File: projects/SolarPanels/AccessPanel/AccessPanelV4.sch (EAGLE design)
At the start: 39 parts

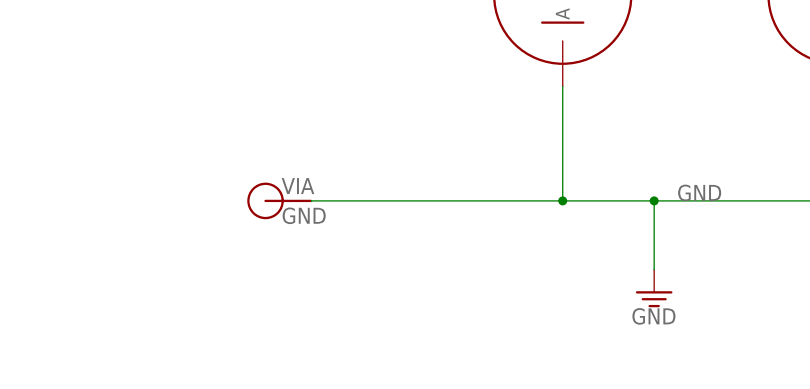
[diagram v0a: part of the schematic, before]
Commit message: Additional edits to Access Panel V4 layout. Just needs the access connector.
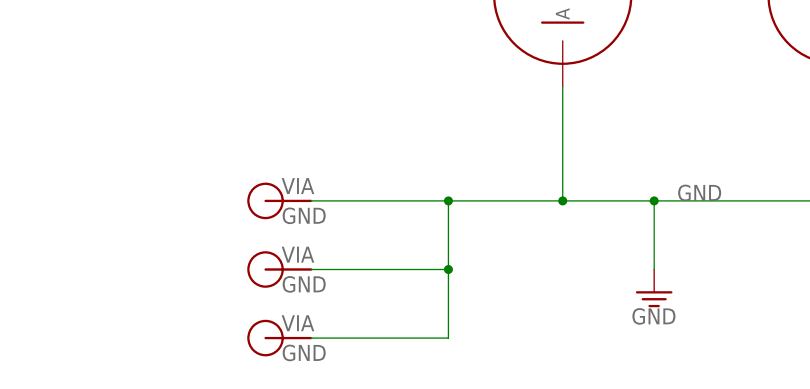
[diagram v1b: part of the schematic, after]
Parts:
- added V2, V5: GND, BrownSpaceEngineering:VIA-60MIL
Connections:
- net GND: now also V2.P$1, V5.P$1
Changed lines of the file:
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@@
 <part name="D1" library="BrownSpaceEngineering" deviceset="DFLS130L" device="" value="DFLS130L"/>
 <part name="R1" library="BrownSpaceEngineering" deviceset="RES" device="1210" value="0R"/>
+<part name="V2" library="BrownSpaceEngineering" deviceset="VIA" device="-60MIL" value="GND"/>
+<part name="V5" library="BrownSpaceEngineering" deviceset="VIA" device="-60MIL" value="GND"/>
 </parts>
 <sheets>
@@
 <instance part="D1" gate="G$1" x="172.72" y="40.64"/>
 <instance part="R1" gate="R$1" x="175.26" y="30.48"/>
+<instance part="V2" gate="G$1" x="-60.96" y="-93.98"/>
+<instance part="V5" gate="G$1" x="-60.96" y="-101.6"/>
 </instances>
 <busses>
@@
 <junction x="127" y="-86.36"/>
 <pinref part="V4" gate="G$1" pin="P$1"/>
-<wire x1="-55.88" y1="-86.36" x2="-27.94" y2="-86.36" width="0.1524" layer="91"/>
+<wire x1="-55.88" y1="-86.36" x2="-40.64" y2="-86.36" width="0.1524" layer="91"/>
 <junction x="-27.94" y="-86.36"/>
 <pinref part="GND1" gate="1" pin="GND"/>
+<wire x1="-40.64" y1="-86.36" x2="-27.94" y2="-86.36" width="0.1524" layer="91"/>
 <wire x1="-17.78" y1="-93.98" x2="-17.78" y2="-86.36" width="0.1524" layer="91"/>
 <junction x="-17.78" y="-86.36"/>
-</segment>
-<segment>
+<pinref part="V5" gate="G$1" pin="P$1"/>
+<wire x1="-55.88" y1="-101.6" x2="-40.64" y2="-101.6" width="0.1524" layer="91"/>
+<wire x1="-40.64" y1="-101.6" x2="-40.64" y2="-93.98" width="0.1524" layer="91"/>
+<junction x="-40.64" y="-86.36"/>
+<pinref part="V2" gate="G$1" pin="P$1"/>
+<wire x1="-40.64" y1="-93.98" x2="-40.64" y2="-86.36" width="0.1524" layer="91"/>
+<wire x1="-55.88" y1="-93.98" x2="-40.64" y2="-93.98" width="0.1524" layer="91"/>
+<junction x="-40.64" y="-93.98"/>
+</segment>
+<segment>

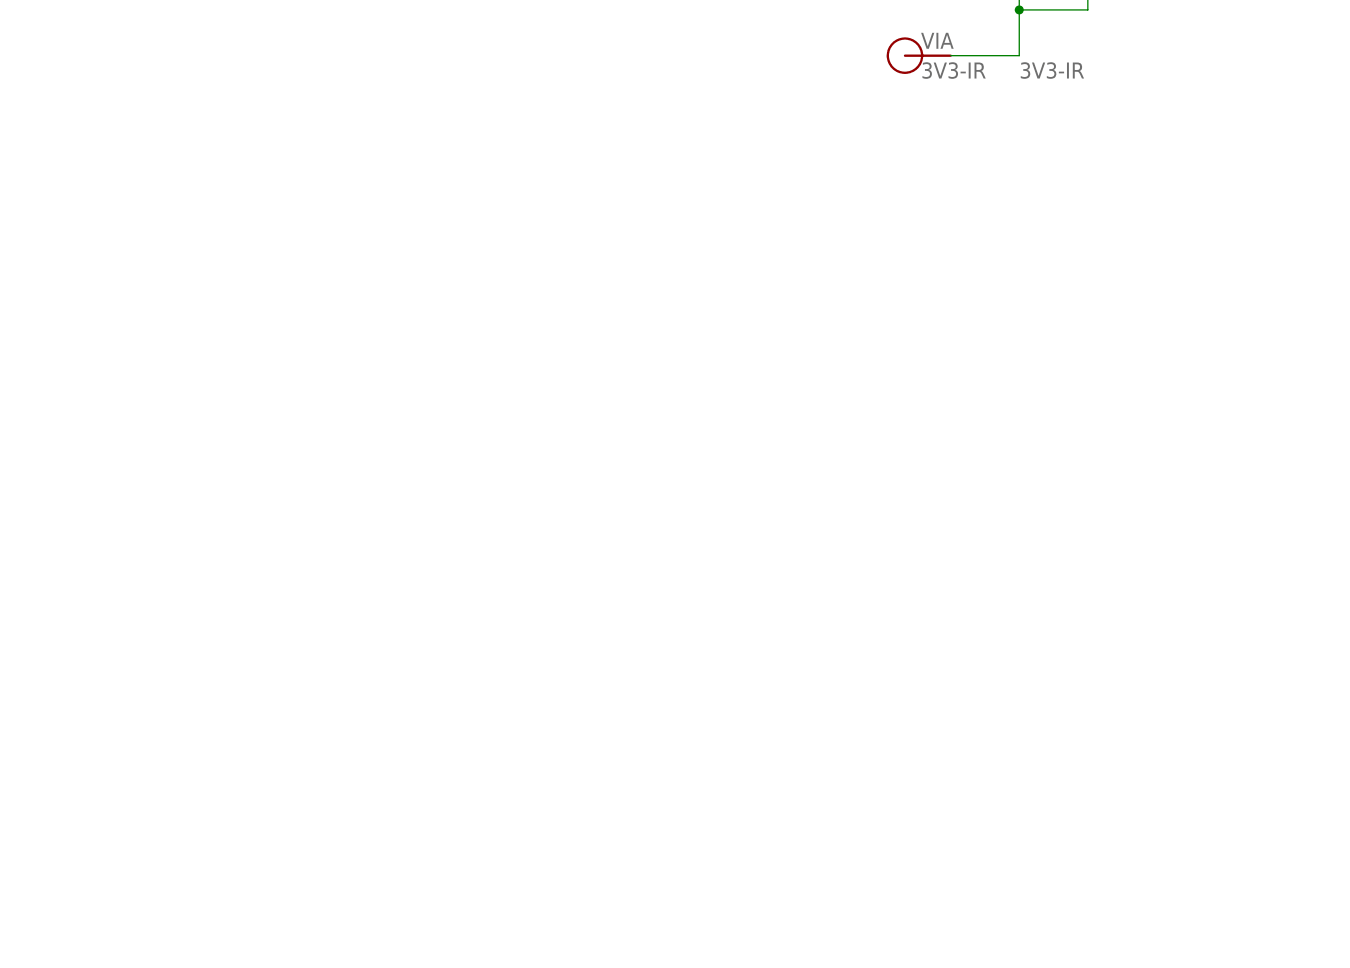
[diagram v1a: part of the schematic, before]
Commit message: Added new access panel connector and completed AccessPanelV4.
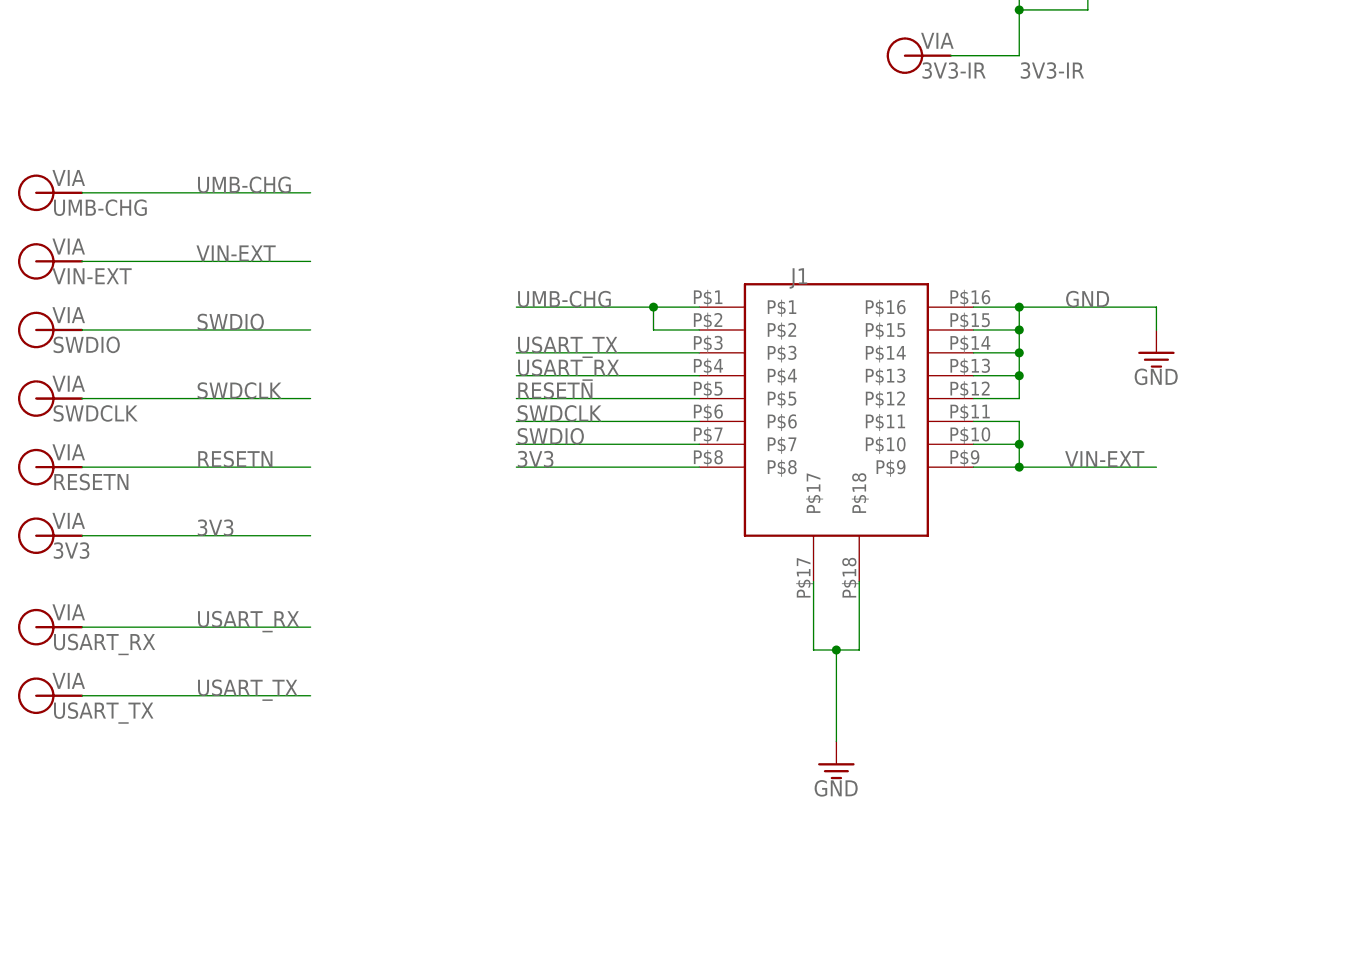
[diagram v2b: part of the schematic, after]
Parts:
- added J1: FFC-16, BrownSpaceEngineering:FFC-16
- added V10: SWDCLK, BrownSpaceEngineering:VIA-60MIL
- added V11: RESETN, BrownSpaceEngineering:VIA-60MIL
- added V14: USART_RX, BrownSpaceEngineering:VIA-60MIL
- added V15: USART_TX, BrownSpaceEngineering:VIA-60MIL
- added V16: 3V3, BrownSpaceEngineering:VIA-60MIL
- added V7: UMB-CHG, BrownSpaceEngineering:VIA-60MIL
- added V8: VIN-EXT, BrownSpaceEngineering:VIA-60MIL
- added V9: SWDIO, BrownSpaceEngineering:VIA-60MIL
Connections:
- new net 3V3: J1.P$8, V16.P$1
- new net RESETN: J1.P$5, V11.P$1
- new net SWDCLK: J1.P$6, V10.P$1
- new net SWDIO: J1.P$7, V9.P$1
- new net UMB-CHG: J1.P$1, J1.P$2, V7.P$1
- new net USART_RX: J1.P$4, V14.P$1
- new net USART_TX: J1.P$3, V15.P$1
- new net VIN-EXT: J1.P$10, J1.P$11, J1.P$9, V8.P$1
- net GND: now also J1.P$12, J1.P$13, J1.P$14, J1.P$15, J1.P$16, J1.P$17, J1.P$18
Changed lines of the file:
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@@
 <part name="V2" library="BrownSpaceEngineering" deviceset="VIA" device="-60MIL" value="GND"/>
 <part name="V5" library="BrownSpaceEngineering" deviceset="VIA" device="-60MIL" value="GND"/>
+<part name="V7" library="BrownSpaceEngineering" deviceset="VIA" device="-60MIL" value="UMB-CHG"/>
+<part name="V8" library="BrownSpaceEngineering" deviceset="VIA" device="-60MIL" value="VIN-EXT"/>
+<part name="V9" library="BrownSpaceEngineering" deviceset="VIA" device="-60MIL" value="SWDIO"/>
+<part name="V10" library="BrownSpaceEngineering" deviceset="VIA" device="-60MIL" value="SWDCLK"/>
+<part name="V11" library="BrownSpaceEngineering" deviceset="VIA" device="-60MIL" value="RESETN"/>
+<part name="V14" library="BrownSpaceEngineering" deviceset="VIA" device="-60MIL" value="USART_RX"/>
+<part name="V15" library="BrownSpaceEngineering" deviceset="VIA" device="-60MIL" value="USART_TX"/>
+<part name="V16" library="BrownSpaceEngineering" deviceset="VIA" device="-60MIL" value="3V3"/>
+<part name="J1" library="BrownSpaceEngineering" deviceset="FFC-16" device=""/>
+<part name="GND3" library="supply1" deviceset="GND" device=""/>
+<part name="GND4" library="supply1" deviceset="GND" device=""/>
 </parts>
 <sheets>
@@
 <instance part="V2" gate="G$1" x="-60.96" y="-93.98"/>
 <instance part="V5" gate="G$1" x="-60.96" y="-101.6"/>
+<instance part="V7" gate="G$1" x="-193.04" y="40.64"/>
+<instance part="V8" gate="G$1" x="-193.04" y="33.02"/>
+<instance part="V9" gate="G$1" x="-193.04" y="25.4"/>
+<instance part="V10" gate="G$1" x="-193.04" y="17.78"/>
+<instance part="V11" gate="G$1" x="-193.04" y="10.16"/>
+<instance part="V14" gate="G$1" x="-193.04" y="-7.62"/>
+<instance part="V15" gate="G$1" x="-193.04" y="-15.24"/>
+<instance part="V16" gate="G$1" x="-193.04" y="2.54"/>
+<instance part="J1" gate="G$1" x="-106.68" y="22.86"/>
+<instance part="GND3" gate="1" x="-104.14" y="-22.86"/>
+<instance part="GND4" gate="1" x="-68.58" y="22.86"/>
 </instances>
 <busses>
@@
 <junction x="-63.5" y="76.2"/>
 </segment>
+<segment>
+<pinref part="J1" gate="G$1" pin="P$17"/>
+<wire x1="-106.68" y1="-2.54" x2="-106.68" y2="-10.16" width="0.1524" layer="91"/>
+<wire x1="-106.68" y1="-10.16" x2="-104.14" y2="-10.16" width="0.1524" layer="91"/>
+<pinref part="J1" gate="G$1" pin="P$18"/>
+<wire x1="-104.14" y1="-10.16" x2="-101.6" y2="-10.16" width="0.1524" layer="91"/>
+<wire x1="-101.6" y1="-10.16" x2="-101.6" y2="-2.54" width="0.1524" layer="91"/>
+<wire x1="-104.14" y1="-10.16" x2="-104.14" y2="-20.32" width="0.1524" layer="91"/>
+<junction x="-104.14" y="-10.16"/>
+<pinref part="GND3" gate="1" pin="GND"/>
+</segment>
+<segment>
+<pinref part="J1" gate="G$1" pin="P$16"/>
+<wire x1="-88.9" y1="27.94" x2="-83.82" y2="27.94" width="0.1524" layer="91"/>
+<wire x1="-83.82" y1="27.94" x2="-68.58" y2="27.94" width="0.1524" layer="91"/>
+<wire x1="-68.58" y1="27.94" x2="-68.58" y2="25.4" width="0.1524" layer="91"/>
+<pinref part="J1" gate="G$1" pin="P$15"/>
+<wire x1="-88.9" y1="25.4" x2="-83.82" y2="25.4" width="0.1524" layer="91"/>
+<wire x1="-83.82" y1="25.4" x2="-83.82" y2="27.94" width="0.1524" layer="91"/>
+<junction x="-83.82" y="27.94"/>
+<pinref part="J1" gate="G$1" pin="P$14"/>
+<wire x1="-88.9" y1="22.86" x2="-83.82" y2="22.86" width="0.1524" layer="91"/>
+<wire x1="-83.82" y1="22.86" x2="-83.82" y2="25.4" width="0.1524" layer="91"/>
+<junction x="-83.82" y="25.4"/>
+<pinref part="J1" gate="G$1" pin="P$13"/>
+<wire x1="-88.9" y1="20.32" x2="-83.82" y2="20.32" width="0.1524" layer="91"/>
+<wire x1="-83.82" y1="20.32" x2="-83.82" y2="22.86" width="0.1524" layer="91"/>
+<junction x="-83.82" y="22.86"/>
+<pinref part="J1" gate="G$1" pin="P$12"/>
+<wire x1="-88.9" y1="17.78" x2="-83.82" y2="17.78" width="0.1524" layer="91"/>
+<wire x1="-83.82" y1="17.78" x2="-83.82" y2="20.32" width="0.1524" layer="91"/>
+<junction x="-83.82" y="20.32"/>
+<label x="-78.74" y="27.94" size="1.778" layer="95"/>
+<pinref part="GND4" gate="1" pin="GND"/>
+</segment>
 </net>
 <net name="SP-PWR" class="0">
@@
 </segment>
 </net>
+<net name="UMB-CHG" class="0">
+<segment>
+<pinref part="V7" gate="G$1" pin="P$1"/>
+<wire x1="-187.96" y1="40.64" x2="-162.56" y2="40.64" width="0.1524" layer="91"/>
+<label x="-175.26" y="40.64" size="1.778" layer="95"/>
+</segment>
+<segment>
+<pinref part="J1" gate="G$1" pin="P$1"/>
+<wire x1="-119.38" y1="27.94" x2="-124.46" y2="27.94" width="0.1524" layer="91"/>
+<pinref part="J1" gate="G$1" pin="P$2"/>
+<wire x1="-124.46" y1="27.94" x2="-139.7" y2="27.94" width="0.1524" layer="91"/>
+<wire x1="-119.38" y1="25.4" x2="-124.46" y2="25.4" width="0.1524" layer="91"/>
+<wire x1="-124.46" y1="25.4" x2="-124.46" y2="27.94" width="0.1524" layer="91"/>
+<junction x="-124.46" y="27.94"/>
+<label x="-139.7" y="27.94" size="1.778" layer="95"/>
+</segment>
+</net>
+<net name="VIN-EXT" class="0">
+<segment>
+<pinref part="V8" gate="G$1" pin="P$1"/>
+<wire x1="-187.96" y1="33.02" x2="-162.56" y2="33.02" width="0.1524" layer="91"/>
+<label x="-175.26" y="33.02" size="1.778" layer="95"/>
+</segment>
+<segment>
+<pinref part="J1" gate="G$1" pin="P$9"/>
+<wire x1="-88.9" y1="10.16" x2="-83.82" y2="10.16" width="0.1524" layer="91"/>
+<pinref part="J1" gate="G$1" pin="P$10"/>
+<wire x1="-83.82" y1="10.16" x2="-68.58" y2="10.16" width="0.1524" layer="91"/>
+<wire x1="-88.9" y1="12.7" x2="-83.82" y2="12.7" width="0.1524" layer="91"/>
+<wire x1="-83.82" y1="12.7" x2="-83.82" y2="10.16" width="0.1524" layer="91"/>
+<junction x="-83.82" y="10.16"/>
+<pinref part="J1" gate="G$1" pin="P$11"/>
+<wire x1="-88.9" y1="15.24" x2="-83.82" y2="15.24" width="0.1524" layer="91"/>
+<wire x1="-83.82" y1="15.24" x2="-83.82" y2="12.7" width="0.1524" layer="91"/>
+<junction x="-83.82" y="12.7"/>
+<label x="-78.74" y="10.16" size="1.778" layer="95"/>
+</segment>
+</net>
+<net name="SWDIO" class="0">
+<segment>
+<pinref part="V9" gate="G$1" pin="P$1"/>
+<wire x1="-187.96" y1="25.4" x2="-162.56" y2="25.4" width="0.1524" layer="91"/>
+<label x="-175.26" y="25.4" size="1.778" layer="95"/>
+</segment>
+<segment>
+<pinref part="J1" gate="G$1" pin="P$7"/>
+<wire x1="-119.38" y1="12.7" x2="-139.7" y2="12.7" width="0.1524" layer="91"/>
+<label x="-139.7" y="12.7" size="1.778" layer="95"/>
+</segment>
+</net>
+<net name="SWDCLK" class="0">
+<segment>
+<pinref part="V10" gate="G$1" pin="P$1"/>
+<wire x1="-187.96" y1="17.78" x2="-162.56" y2="17.78" width="0.1524" layer="91"/>
+<label x="-175.26" y="17.78" size="1.778" layer="95"/>
+</segment>
+<segment>
+<pinref part="J1" gate="G$1" pin="P$6"/>
+<wire x1="-119.38" y1="15.24" x2="-139.7" y2="15.24" width="0.1524" layer="91"/>
+<label x="-139.7" y="15.24" size="1.778" layer="95"/>
+</segment>
+</net>
+<net name="RESETN" class="0">
+<segment>
+<pinref part="V11" gate="G$1" pin="P$1"/>
+<wire x1="-187.96" y1="10.16" x2="-162.56" y2="10.16" width="0.1524" layer="91"/>
+<label x="-175.26" y="10.16" size="1.778" layer="95"/>
+</segment>
+<segment>
+<pinref part="J1" gate="G$1" pin="P$5"/>
+<wire x1="-119.38" y1="17.78" x2="-139.7" y2="17.78" width="0.1524" layer="91"/>
+<label x="-139.7" y="17.78" size="1.778" layer="95"/>
+</segment>
+</net>
+<net name="USART_RX" class="0">
+<segment>
+<pinref part="V14" gate="G$1" pin="P$1"/>
+<wire x1="-187.96" y1="-7.62" x2="-162.56" y2="-7.62" width="0.1524" layer="91"/>
+<label x="-175.26" y="-7.62" size="1.778" layer="95"/>
+</segment>
+<segment>
+<pinref part="J1" gate="G$1" pin="P$4"/>
+<wire x1="-119.38" y1="20.32" x2="-139.7" y2="20.32" width="0.1524" layer="91"/>
+<label x="-139.7" y="20.32" size="1.778" layer="95"/>
+</segment>
+</net>
+<net name="USART_TX" class="0">
+<segment>
+<pinref part="V15" gate="G$1" pin="P$1"/>
+<wire x1="-187.96" y1="-15.24" x2="-162.56" y2="-15.24" width="0.1524" layer="91"/>
+<label x="-175.26" y="-15.24" size="1.778" layer="95"/>
+</segment>
+<segment>
+<pinref part="J1" gate="G$1" pin="P$3"/>
+<wire x1="-119.38" y1="22.86" x2="-139.7" y2="22.86" width="0.1524" layer="91"/>
+<label x="-139.7" y="22.86" size="1.778" layer="95"/>
+</segment>
+</net>
+<net name="3V3" class="0">
+<segment>
+<pinref part="V16" gate="G$1" pin="P$1"/>
+<wire x1="-187.96" y1="2.54" x2="-162.56" y2="2.54" width="0.1524" layer="91"/>
+<label x="-175.26" y="2.54" size="1.778" layer="95"/>
+</segment>
+<segment>
+<pinref part="J1" gate="G$1" pin="P$8"/>
+<wire x1="-119.38" y1="10.16" x2="-139.7" y2="10.16" width="0.1524" layer="91"/>
+<label x="-139.7" y="10.16" size="1.778" layer="95"/>
+</segment>
+</net>
